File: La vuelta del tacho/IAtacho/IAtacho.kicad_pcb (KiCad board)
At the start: 2 copper layers, 8 parts, among them J1 12V de la fuente regulable, J2 5v del step down, J3 motor paso a paso, J4 motor paso a paso, J6 ServoMotor

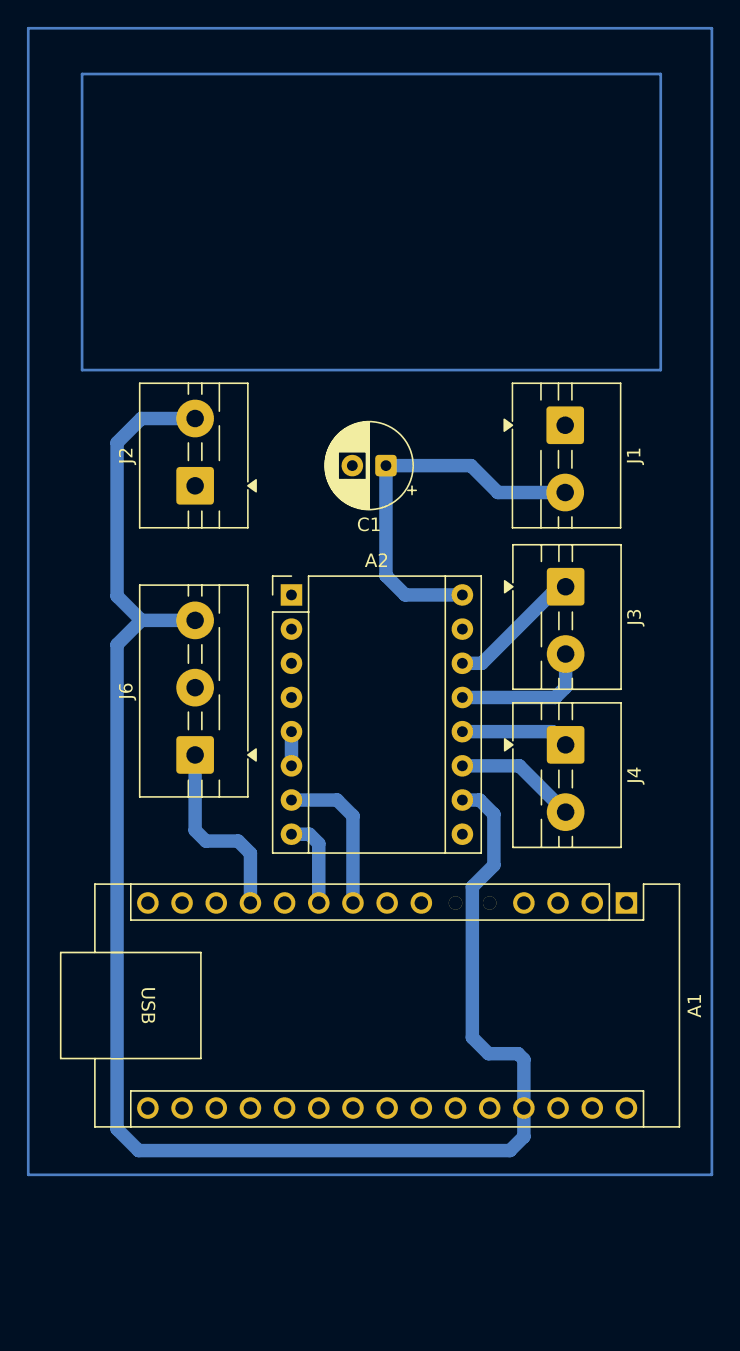
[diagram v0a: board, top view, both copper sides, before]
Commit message: PCB arreglado sin 5v al arduino nano
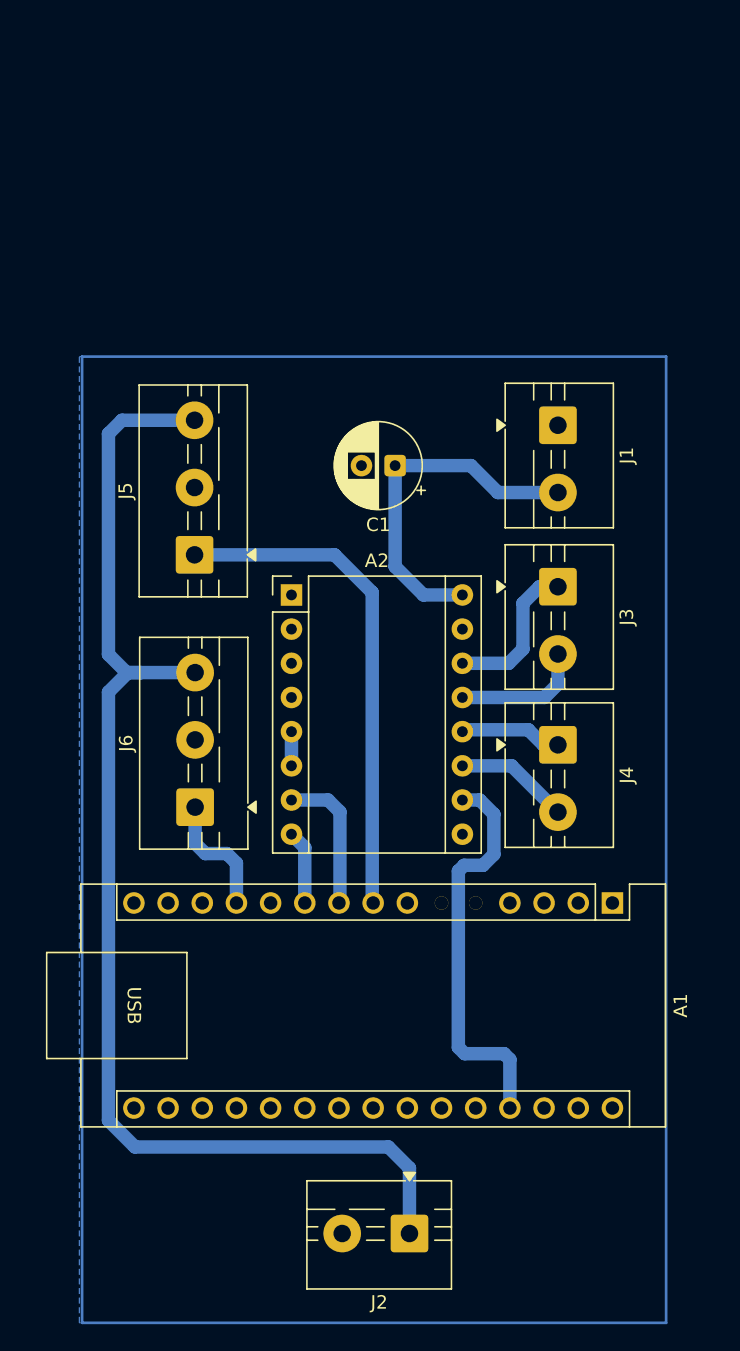
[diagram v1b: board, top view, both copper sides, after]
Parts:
- added J5: Modulo Hall (home), TerminalBlock:TerminalBlock_MaiXu_MX126-5.0-03P_1x03_P5.00mm, F.Cu at (101.4, 76.0)
- moved J2 57.8 mm to (117.4, 126.4), turned to 180 degrees
- moved J6 3.88 mm to (101.4, 94.8)
- moved A1 1.04 mm to (132.4, 101.9)
- moved C1 0.68 mm to (116.3, 69.4)
- moved J3 0.57 mm to (128.4, 78.4)
- moved J4 0.57 mm to (128.4, 90.1)
- moved J1 0.54 mm to (128.4, 66.4)
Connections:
- A1 pad 27: +5V -> 5v
- A1 pad 8: unconnected-(A1-D5-Pad8) -> Señal 
- A2 pad 10: +5V -> 5v
- J2 pad 1: GND -> +5V
- J2 pad 2: +5V -> GND
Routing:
- net Señal : track 0.00 -> 37.5 mm
- net +5V: track 124.6 -> 93.8 mm
- net 5v: track 0.00 -> 29.8 mm
- net Servo: track 14.1 -> 9.33 mm
- net Net-(A2-DIR): track 28.6 -> 26.3 mm
- net B2: track 10.0 -> 11.4 mm
- net Dir: track 6.96 -> 5.75 mm
- net Step: track 11.5 -> 10.8 mm
- net B1: track 10.5 -> 9.74 mm
- net A2: track 9.10 -> 8.52 mm
- net A1: track 8.19 -> 7.62 mm
